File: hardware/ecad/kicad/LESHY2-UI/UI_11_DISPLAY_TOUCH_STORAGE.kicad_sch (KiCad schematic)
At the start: 0 parts

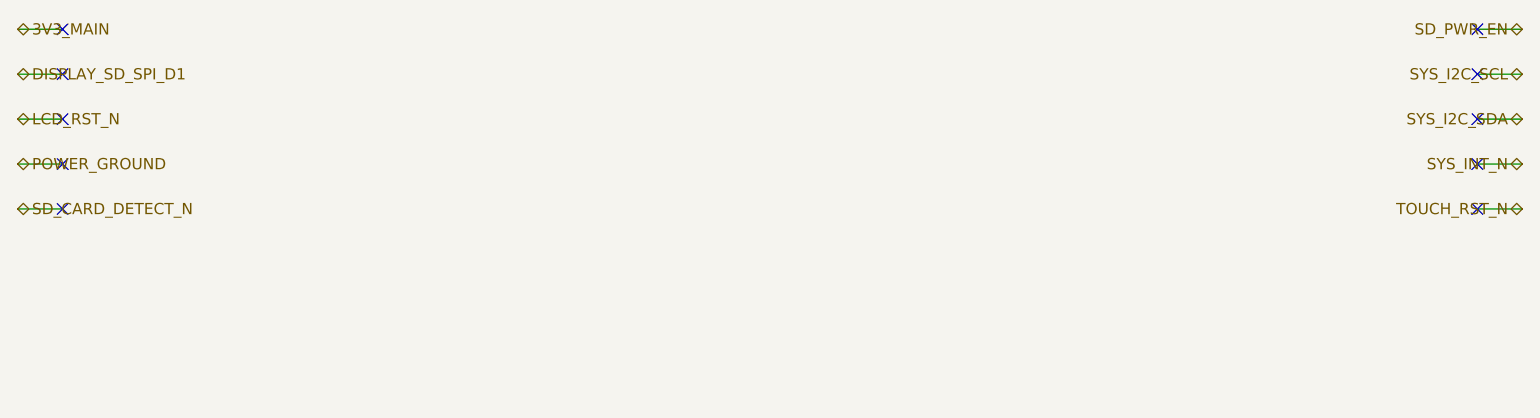
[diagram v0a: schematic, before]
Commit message: Complete H2.2.2 S3 core schematic
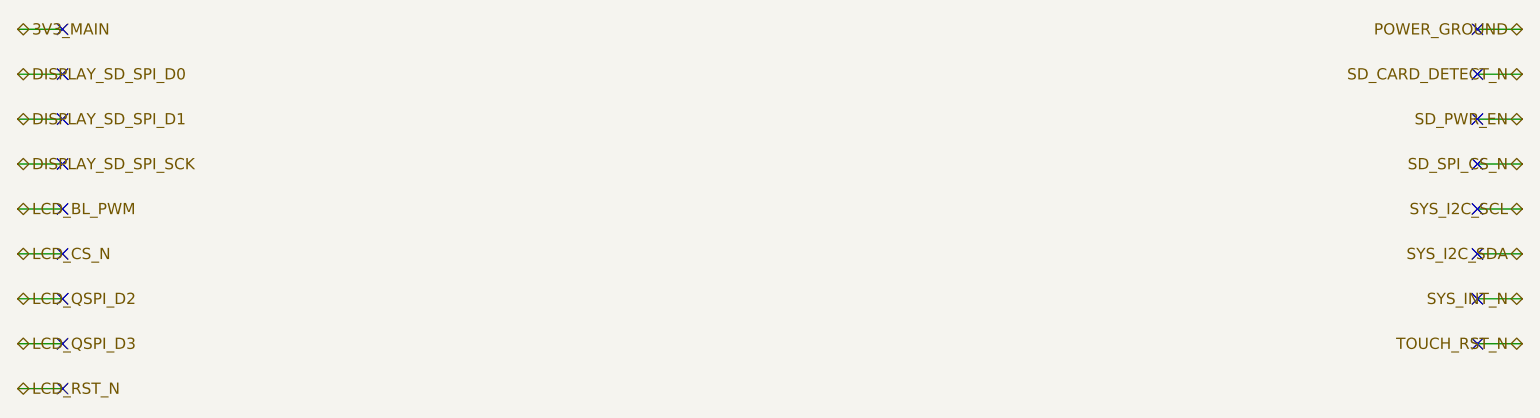
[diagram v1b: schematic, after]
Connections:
- no-connect marks 10 -> 17
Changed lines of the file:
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@@
 	(no_connect (at 25.40 20.32)
 	)
-	(hierarchical_label "DISPLAY_SD_SPI_D1"
+	(hierarchical_label "DISPLAY_SD_SPI_D0"
 		(shape bidirectional)
 		(at 20.32 25.40 0)
@@
 	(no_connect (at 25.40 25.40)
 	)
-	(hierarchical_label "LCD_RST_N"
+	(hierarchical_label "DISPLAY_SD_SPI_D1"
 		(shape bidirectional)
 		(at 20.32 30.48 0)
@@
 	(no_connect (at 25.40 30.48)
 	)
-	(hierarchical_label "POWER_GROUND"
+	(hierarchical_label "DISPLAY_SD_SPI_SCK"
 		(shape bidirectional)
 		(at 20.32 35.56 0)
@@
 	(no_connect (at 25.40 35.56)
 	)
-	(hierarchical_label "SD_CARD_DETECT_N"
+	(hierarchical_label "LCD_BL_PWM"
 		(shape bidirectional)
 		(at 20.32 40.64 0)
@@
 	(no_connect (at 25.40 40.64)
 	)
-	(hierarchical_label "SD_PWR_EN"
+	(hierarchical_label "LCD_CS_N"
+		(shape bidirectional)
+		(at 20.32 45.72 0)
+		(effects (font (size 1.27 1.27)))
+	)
+	(wire
+		(pts (xy 20.32 45.72) (xy 25.40 45.72))
+		(stroke (width 0) (type default))
+	)
+	(no_connect (at 25.40 45.72)
+	)
+	(hierarchical_label "LCD_QSPI_D2"
+		(shape bidirectional)
+		(at 20.32 50.80 0)
+		(effects (font (size 1.27 1.27)))
+	)
+	(wire
+		(pts (xy 20.32 50.80) (xy 25.40 50.80))
+		(stroke (width 0) (type default))
+	)
+	(no_connect (at 25.40 50.80)
+	)
+	(hierarchical_label "LCD_QSPI_D3"
+		(shape bidirectional)
+		(at 20.32 55.88 0)
+		(effects (font (size 1.27 1.27)))
+	)
+	(wire
+		(pts (xy 20.32 55.88) (xy 25.40 55.88))
+		(stroke (width 0) (type default))
+	)
+	(no_connect (at 25.40 55.88)
+	)
+	(hierarchical_label "LCD_RST_N"
+		(shape bidirectional)
+		(at 20.32 60.96 0)
+		(effects (font (size 1.27 1.27)))
+	)
+	(wire
+		(pts (xy 20.32 60.96) (xy 25.40 60.96))
+		(stroke (width 0) (type default))
+	)
+	(no_connect (at 25.40 60.96)
+	)
+	(hierarchical_label "POWER_GROUND"
 		(shape bidirectional)
 		(at 190.50 20.32 180)
@@
 	(no_connect (at 185.42 20.32)
 	)
-	(hierarchical_label "SYS_I2C_SCL"
+	(hierarchical_label "SD_CARD_DETECT_N"
 		(shape bidirectional)
 		(at 190.50 25.40 180)
@@
 	(no_connect (at 185.42 25.40)
 	)
-	(hierarchical_label "SYS_I2C_SDA"
+	(hierarchical_label "SD_PWR_EN"
 		(shape bidirectional)
 		(at 190.50 30.48 180)
@@
 	(no_connect (at 185.42 30.48)
 	)
-	(hierarchical_label "SYS_INT_N"
+	(hierarchical_label "SD_SPI_CS_N"
 		(shape bidirectional)
 		(at 190.50 35.56 180)
@@
 	(no_connect (at 185.42 35.56)
 	)
-	(hierarchical_label "TOUCH_RST_N"
+	(hierarchical_label "SYS_I2C_SCL"
 		(shape bidirectional)
 		(at 190.50 40.64 180)
@@
 	(no_connect (at 185.42 40.64)
 	)
+	(hierarchical_label "SYS_I2C_SDA"
+		(shape bidirectional)
+		(at 190.50 45.72 180)
+		(effects (font (size 1.27 1.27)) (justify right))
+	)
+	(wire
+		(pts (xy 190.50 45.72) (xy 185.42 45.72))
+		(stroke (width 0) (type default))
+	)
+	(no_connect (at 185.42 45.72)
+	)
+	(hierarchical_label "SYS_INT_N"
+		(shape bidirectional)
+		(at 190.50 50.80 180)
+		(effects (font (size 1.27 1.27)) (justify right))
+	)
+	(wire
+		(pts (xy 190.50 50.80) (xy 185.42 50.80))
+		(stroke (width 0) (type default))
+	)
+	(no_connect (at 185.42 50.80)
+	)
+	(hierarchical_label "TOUCH_RST_N"
+		(shape bidirectional)
+		(at 190.50 55.88 180)
+		(effects (font (size 1.27 1.27)) (justify right))
+	)
+	(wire
+		(pts (xy 190.50 55.88) (xy 185.42 55.88))
+		(stroke (width 0) (type default))
+	)
+	(no_connect (at 185.42 55.88)
+	)
 	(sheet_instances

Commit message: Complete H2.2.3 display touch storage schematic
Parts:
- added C1: TDK C1005X7R1H104K050BB, Capacitor_SMD:C_0402_1005Metric, symbol Leshy2:UI11_TOUCH_IRQ_BUFFER_BYPASS
- added C10: TDK C1005X7R1H104K050BB, Capacitor_SMD:C_0402_1005Metric, symbol Leshy2:UI11_SD_MISO_BUFFER_BYPASS
- added C11: TDK C1005X7R1H104K050BB, Capacitor_SMD:C_0402_1005Metric, symbol Leshy2:UI11_SD_DETECT_CAP
- added C2: Murata GRM188R60J106ME47D, Capacitor_SMD:C_0603_1608Metric, symbol Leshy2:UI11_DISPLAY_LOGIC_BULK_CAP
- added C3: TDK C1005X7R1H104K050BB, Capacitor_SMD:C_0402_1005Metric, symbol Leshy2:UI11_DISPLAY_LOGIC_HF_CAP
- added C4: TDK C1005X7R1H104K050BB, Capacitor_SMD:C_0402_1005Metric, symbol Leshy2:UI11_BACKLIGHT_EFUSE_INPUT_CAP
- added C5: Murata GRM188R60J106ME47D, Capacitor_SMD:C_0603_1608Metric, symbol Leshy2:UI11_BACKLIGHT_EFUSE_OUTPUT_BULK
- added C6: TDK C1608X7R1C105K080AC, Capacitor_SMD:C_0603_1608Metric, symbol Leshy2:UI11_SD_POWER_INPUT_CAP
- added C7: Murata GRM21BR60J226ME39L, Capacitor_SMD:C_0805_2012Metric, symbol Leshy2:UI11_SD_POWER_BULK_CAP
- added C8: TDK C1005X7R1H104K050BB, Capacitor_SMD:C_0402_1005Metric, symbol Leshy2:UI11_SD_POWER_HF_CAP
- added C9: TDK C1005X7R1H104K050BB, Capacitor_SMD:C_0402_1005Metric, symbol Leshy2:UI11_SD_HOST_BUFFER_BYPASS
- added J1: Hirose DM3AT-SF-PEJM5, Connector_Card:microSD_HC_Hirose_DM3AT-SF-PEJM5, symbol Leshy2:UI11_SD
- added J2: Hirose DF40C(2.0)-40DS-0.4V(58), Connector_Hirose_DF40:Hirose_DF40C(2.0)-40DS-0.4V_2x20_P0.4mm, symbol Leshy2:UI11_DISPLAY_CONNECTOR
- added R1: Yageo RC0402FR-0710KL, Resistor_SMD:R_0402_1005Metric, symbol Leshy2:UI11_TOUCH_IRQ_PULLUP
- added R10: Yageo RC0402FR-0710KL, Resistor_SMD:R_0402_1005Metric, symbol Leshy2:UI11_SD_HOST_SCK_PULLDOWN
- added R11: Yageo RC0402FR-0710KL, Resistor_SMD:R_0402_1005Metric, symbol Leshy2:UI11_SD_HOST_D0_PULLDOWN
- added R12: Yageo RC0402FR-0710KL, Resistor_SMD:R_0402_1005Metric, symbol Leshy2:UI11_SD_HOST_D1_PULLUP
- added R13: Yageo RC0402FR-0710KL, Resistor_SMD:R_0402_1005Metric, symbol Leshy2:UI11_SD_HOST_CS_PULLUP
- added R14: Yageo RC0402FR-0710KL, Resistor_SMD:R_0402_1005Metric, symbol Leshy2:UI11_LCD_HOST_CS_PULLUP
- added R15: Yageo RC0402FR-0710KL, Resistor_SMD:R_0402_1005Metric, symbol Leshy2:UI11_SD_CARD_CMD_PULLUP
- added R16: Yageo RC0402FR-0710KL, Resistor_SMD:R_0402_1005Metric, symbol Leshy2:UI11_SD_CARD_DAT0_PULLUP
- added R17: Yageo RC0402FR-0710KL, Resistor_SMD:R_0402_1005Metric, symbol Leshy2:UI11_SD_CARD_DAT1_PULLUP
- added R18: Yageo RC0402FR-0710KL, Resistor_SMD:R_0402_1005Metric, symbol Leshy2:UI11_SD_CARD_DAT2_PULLUP
- added R19: Yageo RC0402FR-0710KL, Resistor_SMD:R_0402_1005Metric, symbol Leshy2:UI11_SD_CARD_DAT3_PULLUP
- added R2: Yageo RC0402FR-0710KL, Resistor_SMD:R_0402_1005Metric, symbol Leshy2:UI11_DISPLAY_RESET_PULLDOWN
- added R20: Panasonic ERJ-2RKF22R0X, Resistor_SMD:R_0402_1005Metric, symbol Leshy2:UI11_SD_SCK_SERIES
- added R21: Panasonic ERJ-2RKF22R0X, Resistor_SMD:R_0402_1005Metric, symbol Leshy2:UI11_SD_CMD_SERIES
- added R22: Panasonic ERJ-2RKF22R0X, Resistor_SMD:R_0402_1005Metric, symbol Leshy2:UI11_SD_CS_SERIES
- added R23: Panasonic ERJ-2RKF22R0X, Resistor_SMD:R_0402_1005Metric, symbol Leshy2:UI11_SD_MISO_SERIES
- added R24: Yageo RC0603FR-071KL, Resistor_SMD:R_0603_1608Metric, symbol Leshy2:UI11_SD_DETECT_SERIES
- added R25: Yageo RC0402FR-0710KL, Resistor_SMD:R_0402_1005Metric, symbol Leshy2:UI11_SD_DETECT_PULLUP
- added R3: Yageo RC0402FR-0710KL, Resistor_SMD:R_0402_1005Metric, symbol Leshy2:UI11_TOUCH_RESET_PULLDOWN
- added R4: Yageo RC0402FR-07133KL, Resistor_SMD:R_0402_1005Metric, symbol Leshy2:UI11_BACKLIGHT_EFUSE_ILIM
- added R5: Yageo RC0402FR-0710KL, Resistor_SMD:R_0402_1005Metric, symbol Leshy2:UI11_BACKLIGHT_FAULT_PULLUP
- added R6: Panasonic ERJ-P08F10R0V, Resistor_SMD:R_1206_3216Metric, symbol Leshy2:UI11_BACKLIGHT_SERIES_RESISTOR
- added R7: Yageo RC0402FR-07100RL, Resistor_SMD:R_0402_1005Metric, symbol Leshy2:UI11_BACKLIGHT_GATE_SERIES
- added R8: Yageo RC0402FR-0710KL, Resistor_SMD:R_0402_1005Metric, symbol Leshy2:UI11_BACKLIGHT_GATE_PULLDOWN
- added R9: Yageo RC0402FR-0710KL, Resistor_SMD:R_0402_1005Metric, symbol Leshy2:UI11_SD_ON_PULLDOWN
- added U1: SN74LVC1G07DCKR, Package_TO_SOT_SMD:Texas_R-PDSO-G5_DCK-5, symbol Leshy2:UI11_TOUCH_IRQ_BUFFER
- added U2: Texas Instruments TPS2553DRVR-1, Package_SON:WSON-6-1EP_2x2mm_P0.65mm_EP1x1.6mm, symbol Leshy2:UI11_BACKLIGHT_EFUSE
- added U3: TDK C1005X7R1H104K050BB, Capacitor_SMD:C_0402_1005Metric, symbol Leshy2:UI11_BACKLIGHT_EFUSE_OUTPUT_HF
- added U4: Diodes Incorporated DMN2056U-7, Package_TO_SOT_SMD:SOT-23, symbol Leshy2:UI11_BACKLIGHT_MOSFET
- added U5: SN74LVC3G34DCUR, Package_SO:VSSOP-8_2.3x2mm_P0.5mm, symbol Leshy2:UI11_SD_HOST_BUFFER
- added U6: Texas Instruments SN74LVC1G125DCKR, Package_TO_SOT_SMD:Texas_R-PDSO-G5_DCK-5, symbol Leshy2:UI11_SD_MISO_BUFFER
- added U7: Texas Instruments TPD4E05U06DQAR, Package_SON:USON-10_2.5x1.0mm_P0.5mm, symbol Leshy2:UI11_SD_ESD_A
- added U8: Texas Instruments TPD4E05U06DQAR, Package_SON:USON-10_2.5x1.0mm_P0.5mm, symbol Leshy2:UI11_SD_ESD_B
- added U9: Texas Instruments TPS22919DCKR, Package_TO_SOT_SMD:SOT-363_SC-70-6, symbol Leshy2:UI11_SD_POWER_SWITCH
- added X1: Sitronix ST77922, symbol Leshy2:UI11_DISPLAY_TOUCH_CONTROLLER
- added X2: HMX035CTFT-001 (QDtech schematic assembly marking), symbol Leshy2:UI11_DISPLAY
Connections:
- net 3V3_MAIN: now also C1.1 (END_1), C2.1 (END_1), C3.1 (END_1), C4.1 (END_1), C6.1 (END_1), J2.39 (PIN_39), J2.6 (PIN_6), J2.7 (PIN_7), R1.1 (END_1), R12.2 (END_2), R13.2 (END_2), R14.2 (END_2), R25.1 (END_1), R5.1 (END_1), U1.5 (VCC), U2.4 (EN), U2.6 (IN), U9.1 (IN), X1.IM1P, X1.VDD, X1.VDDI, X2.39 (IM1), X2.6 (VDDI), X2.7 (VDD)
- net DISPLAY_SD_SPI_D0: now also J2.13 (PIN_13), R11.1 (END_1), U5.3 (2A), X1.QSPI_D0_SDA, X2.13 (QSPI_D0)
- net DISPLAY_SD_SPI_D1: now also J2.10 (PIN_10), R12.1 (END_1), R23.2 (END_2), X1.QSPI_D1_DCX, X2.10 (QSPI_D1)
- net DISPLAY_SD_SPI_SCK: now also J2.11 (PIN_11), R10.1 (END_1), U5.1 (1A), X1.QSPI_SCL_RDX, X2.11 (QSPI_CLK)
- net LCD_BL_PWM: now also R7.1 (END_1)
- net LCD_CS_N: now also J2.9 (PIN_9), R14.1 (END_1), X1.CSX, X2.9 (QSPI_CS)
- net LCD_QSPI_D2: now also J2.17 (PIN_17), X1.QSPI_D2_D0, X2.17 (QSPI_D2)
- net LCD_QSPI_D3: now also J2.18 (PIN_18), X1.QSPI_D3_D1, X2.18 (QSPI_D3)
- net LCD_RST_N: now also J2.15 (PIN_15), R2.1 (END_1), X1.RESX, X2.15 (RESET)
- net POWER_GROUND: now also C1.2 (END_2), C10.2 (END_2), C11.2 (END_2), C2.2 (END_2), C3.2 (END_2), C4.2 (END_2), C5.2 (END_2), C6.2 (END_2), C7.2 (END_2), C8.2 (END_2), C9.2 (END_2), J1.10 (DETECT_B), J1.6 (VSS), J1.SH (SHIELD), J2.16 (PIN_16), J2.19 (PIN_19), J2.20 (PIN_20), J2.21 (PIN_21), J2.22 (PIN_22), J2.23 (PIN_23), J2.24 (PIN_24), J2.37 (PIN_37), J2.38 (PIN_38), J2.40 (PIN_40), J2.5 (PIN_5), R10.2 (END_2), R11.2 (END_2), R2.2 (END_2), R3.2 (END_2), R4.2 (END_2), R8.2 (END_2), R9.2 (END_2), U1.3 (GND), U2.5 (GND), U2.7 (POWERPAD), U3.2 (END_2), U4.2 (S), U5.4 (GND), U6.3 (GND), U7.3 (GND_3), U7.8 (GND_8), U8.3 (GND_3), U8.8 (GND_8), U9.2 (GND), X1.GND, X1.IM0P, X1.IM2P, X2.16 (GND_16), X2.19 (DB2_STRAP), X2.20 (DB3_STRAP), X2.21 (DB4_STRAP), X2.22 (DB5_STRAP), X2.23 (DB6_STRAP), X2.24 (DB7_STRAP), X2.37 (GND_37), X2.38 (IM0), X2.40 (IM2), X2.5 (GND_5)
- net SD_CARD_DETECT_N: now also C11.1 (END_1), R24.2 (END_2), R25.2 (END_2)
- net SD_PWR_EN: now also R9.1 (END_1), U9.3 (ON)
- net SD_SPI_CS_N: now also R13.1 (END_1), U5.6 (3A), U6.1 (OE_N)
- net SYS_I2C_SCL: now also J2.1 (PIN_1), X1.TP_I2C_SCL, X2.1 (TP_I2C_SCL)
- net SYS_I2C_SDA: now also J2.2 (PIN_2), X1.TP_I2C_SDA, X2.2 (TP_I2C_SDA)
- net SYS_INT_N: now also U1.4 (Y)
- net TOUCH_RST_N: now also J2.4 (PIN_4), R3.1 (END_1), X1.TP_RESXP, X2.4 (TP_RESET)
- new net LCD_BACKLIGHT_FAULT_N: R5.2 (END_2), U2.3 (FAULT_N)
- new net LCD_BACKLIGHT_GATE: R7.2 (END_2), R8.1 (END_1), U4.1 (G)
- new net LCD_BACKLIGHT_ILIM: R4.1 (END_1), U2.2 (ILIM)
- new net LCD_LEDA_PROTECTED: C5.1 (END_1), J2.33 (PIN_33), U2.1 (OUT), U3.1 (END_1), X2.33 (LEDA)
- new net LCD_LEDK: J2.34 (PIN_34), J2.35 (PIN_35), J2.36 (PIN_36), R6.1 (END_1), X2.34 (LEDK_1), X2.35 (LEDK_2), X2.36 (LEDK_3)
- new net LCD_LEDK_LIMITED: R6.2 (END_2), U4.3 (D)
- new net LCD_TOUCH_INT_RAW_N: J2.3 (PIN_3), R1.2 (END_2), U1.2 (A), X1.TP_INT, X2.3 (TP_INT)
- new net SD_CARD_3V3: C10.1 (END_1), C7.1 (END_1), C8.1 (END_1), C9.1 (END_1), J1.4 (VDD), R15.1 (END_1), R16.1 (END_1), R17.1 (END_1), R18.1 (END_1), R19.1 (END_1), U5.8 (VCC), U6.5 (VCC), U8.4 (D2_PLUS), U9.5 (QOD), U9.6 (VOUT)
- new net SD_CARD_DETECT_RAW_N: J1.9 (DETECT_A), R24.1 (END_1), U8.5 (D2_MINUS)
- new net SD_CLK_BUFFERED: R20.1 (END_1), U5.7 (1Y)
- new net SD_CLK_PROTECTED: J1.5 (CLK), R20.2 (END_2), U7.1 (D1_PLUS)
- new net SD_CMD_BUFFERED: R21.1 (END_1), U5.5 (2Y)
- new net SD_CMD_PROTECTED: J1.3 (CMD), R15.2 (END_2), R21.2 (END_2), U7.2 (D1_MINUS)
- new net SD_CS_BUFFERED_N: R22.1 (END_1), U5.2 (3Y)
- new net SD_DAT0_MISO_PROTECTED: J1.7 (DAT0), R16.2 (END_2), U6.2 (A), U7.5 (D2_MINUS)
- new net SD_DAT1_PROTECTED: J1.8 (DAT1), R17.2 (END_2), U8.1 (D1_PLUS)
- new net SD_DAT2_PROTECTED: J1.1 (DAT2), R18.2 (END_2), U8.2 (D1_MINUS)
- new net SD_DAT3_CS_PROTECTED_N: J1.2 (CD_DAT3), R19.2 (END_2), R22.2 (END_2), U7.4 (D2_PLUS)
- new net SD_MISO_BUFFERED: R23.1 (END_1), U6.4 (Y)
- no-connect marks 17 -> 33
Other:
- title: (none) -> Leshy2 — exact display, integrated touch and isolated microSD

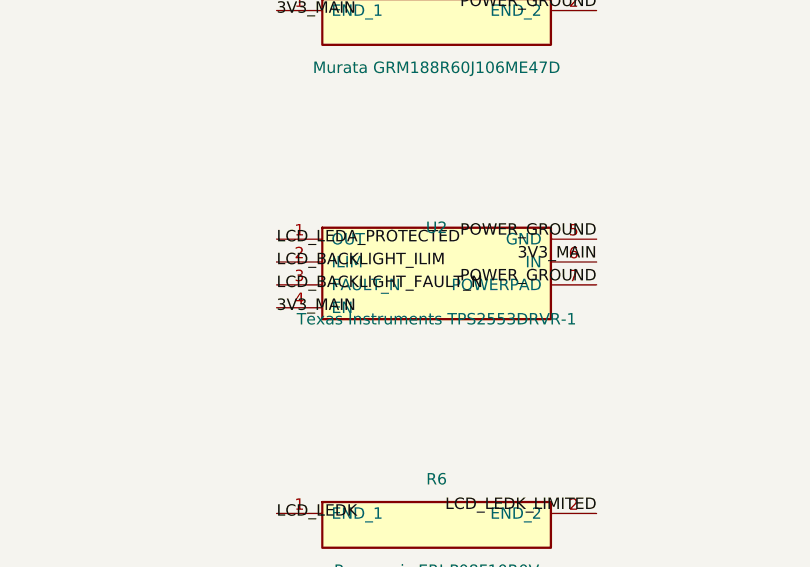
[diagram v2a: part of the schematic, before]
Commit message: complete exact H2.2.10 UI test points
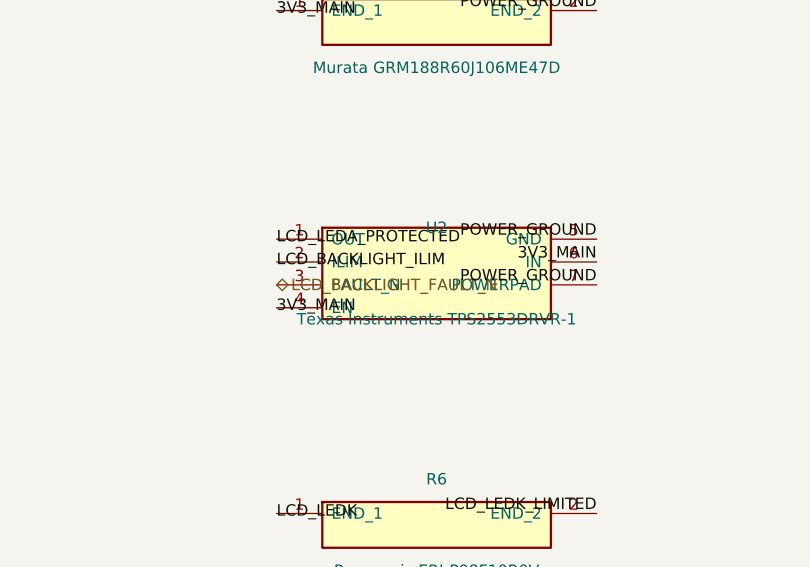
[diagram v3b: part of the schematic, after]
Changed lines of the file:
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@@
 		(effects (font (size 1.27 1.27)))
 	)
-	(label "LCD_BACKLIGHT_FAULT_N"
+	(hierarchical_label "LCD_BACKLIGHT_FAULT_N"
+		(shape bidirectional)
 		(at 276.86 99.06 0)
 		(effects (font (size 1.27 1.27)))

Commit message: complete H2 schematic review package
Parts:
- renumbered C1 to C11001, C2 to C11002, C3 to C11003, C4 to C11004, C5 to C11005, C6 to C11006, C7 to C11007, C8 to C11008, C9 to C11009, C10 to C11010, C11 to C11011, J1 to J11001, J2 to J11002, R1 to R11001, R2 to R11002, R3 to R11003, R4 to R11004, R5 to R11005, R6 to R11006, R7 to R11007, R8 to R11008, R9 to R11009, R10 to R11010, R11 to R11011, R12 to R11012, R13 to R11013, R14 to R11014, R15 to R11015, R16 to R11016, R17 to R11017, R18 to R11018, R19 to R11019, R20 to R11020, R21 to R11021, R22 to R11022, R23 to R11023, R24 to R11024, R25 to R11025, U1 to U11001, U2 to U11002, U3 to U11003, U4 to U11004, U5 to U11005, U6 to U11006, U7 to U11007, U8 to U11008, U9 to U11009, X1 to X11001, X2 to X11002

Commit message: Complete H3.3.1 display electrical verification
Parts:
- R11006: value Panasonic ERJ-P08F10R0V -> Yageo RC0402JR-070RL; footprint Resistor_SMD:R_1206_3216Metric -> Resistor_SMD:R_0402_1005Metric
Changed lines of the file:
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@@
 			(effects (font (size 1.27 1.27)))
 		)
-		(property "Value" "Panasonic ERJ-P08F10R0V"
+		(property "Value" "Yageo RC0402JR-070RL"
 			(at 294.64 130.81 0)
 			(show_name no)
@@
 			(effects (font (size 1.27 1.27)))
 		)
-		(property "Footprint" "Resistor_SMD:R_1206_3216Metric"
+		(property "Footprint" "Resistor_SMD:R_0402_1005Metric"
 			(at 294.64 125.73 0)
 			(show_name no)
@@
 			(effects (font (size 1.27 1.27)))
 		)
-		(property "Description" "10ohm_1pct_1206_0_66w_anti_surge_power_resistor"
+		(property "Description" "0ohm_0402_jumper_resistor"
 			(at 294.64 125.73 0)
 			(show_name no)

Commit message: Optimize H1 display and stocked BOM routes
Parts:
- C11001, C11003, C11004, C11008, C11009, C11010, C11011, U11003: value TDK C1005X7R1H104K050BB -> Yageo CC0402KRX7R9BB104
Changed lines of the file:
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@@
 			(effects (font (size 1.27 1.27)))
 		)
-		(property "Value" "TDK C1005X7R1H104K050BB"
+		(property "Value" "Yageo CC0402KRX7R9BB104"
 			(at 294.64 49.53 0)
 			(show_name no)
@@
 			(effects (font (size 1.27 1.27)))
 		)
-		(property "Description" "40-contact fixed receptacle for the replaceable display adapter"
+		(property "Description" "40-contact fixed receptacle for the antenna-edge replaceable display adapter"
 			(at 213.36 92.71 0)
 			(show_name no)
@@
 			(effects (font (size 1.27 1.27)))
 		)
-		(property "Value" "TDK C1005X7R1H104K050BB"
+		(property "Value" "Yageo CC0402KRX7R9BB104"
 			(at 132.08 77.47 0)
 			(show_name no)
@@
 			(effects (font (size 1.27 1.27)))
 		)
-		(property "Value" "TDK C1005X7R1H104K050BB"
+		(property "Value" "Yageo CC0402KRX7R9BB104"
 			(at 375.92 113.03 0)
 			(show_name no)
@@
 			(effects (font (size 1.27 1.27)))
 		)
-		(property "Value" "TDK C1005X7R1H104K050BB"
+		(property "Value" "Yageo CC0402KRX7R9BB104"
 			(at 457.20 120.65 0)
 			(show_name no)
@@
 			(effects (font (size 1.27 1.27)))
 		)
-		(property "Value" "TDK C1005X7R1H104K050BB"
+		(property "Value" "Yageo CC0402KRX7R9BB104"
 			(at 457.20 176.53 0)
 			(show_name no)
@@
 			(effects (font (size 1.27 1.27)))
 		)
-		(property "Value" "TDK C1005X7R1H104K050BB"
+		(property "Value" "Yageo CC0402KRX7R9BB104"
 			(at 132.08 181.61 0)
 			(show_name no)
@@
 			(effects (font (size 1.27 1.27)))
 		)
-		(property "Value" "TDK C1005X7R1H104K050BB"
+		(property "Value" "Yageo CC0402KRX7R9BB104"
 			(at 294.64 189.23 0)
 			(show_name no)
@@
 			(effects (font (size 1.27 1.27)))
 		)
-		(property "Value" "TDK C1005X7R1H104K050BB"
+		(property "Value" "Yageo CC0402KRX7R9BB104"
 			(at 294.64 265.43 0)
 			(show_name no)

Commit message: Replace six pre-order resistor identities
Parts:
- R11004: value Yageo RC0402FR-07133KL -> UNI-ROYAL 0402WGF1333TCE
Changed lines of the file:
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@@
 			(effects (font (size 1.27 1.27)))
 		)
-		(property "Value" "Yageo RC0402FR-07133KL"
+		(property "Value" "UNI-ROYAL 0402WGF1333TCE"
 			(at 132.08 102.87 0)
 			(show_name no)

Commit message: Reduce factory BOM cost without functional loss
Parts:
- J11002: value Hirose DF40C(2.0)-40DS-0.4V(58) -> Hirose DF40C(2.0)-40DS-0.4V(51)
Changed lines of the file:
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@@
 			(effects (font (size 1.27 1.27)))
 		)
-		(property "Value" "Hirose DF40C(2.0)-40DS-0.4V(58)"
+		(property "Value" "Hirose DF40C(2.0)-40DS-0.4V(51)"
 			(at 213.36 120.71 0)
 			(show_name no)
